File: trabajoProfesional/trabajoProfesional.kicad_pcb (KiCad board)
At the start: 2 copper layers, 66.2 x 25.4 mm, 47 parts, among them T1 MPMOS, U1 1501

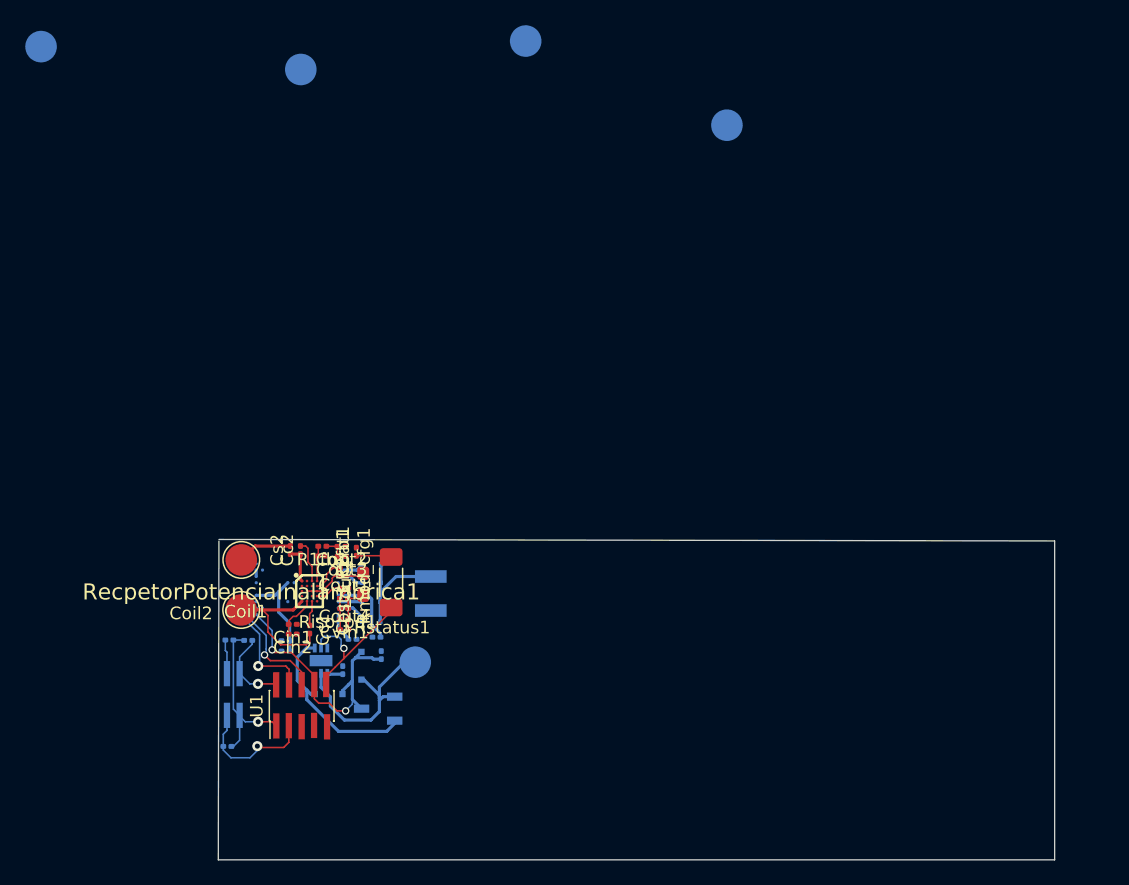
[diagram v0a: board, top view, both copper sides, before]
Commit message: fue todo a doble capa con componentes de dos lados
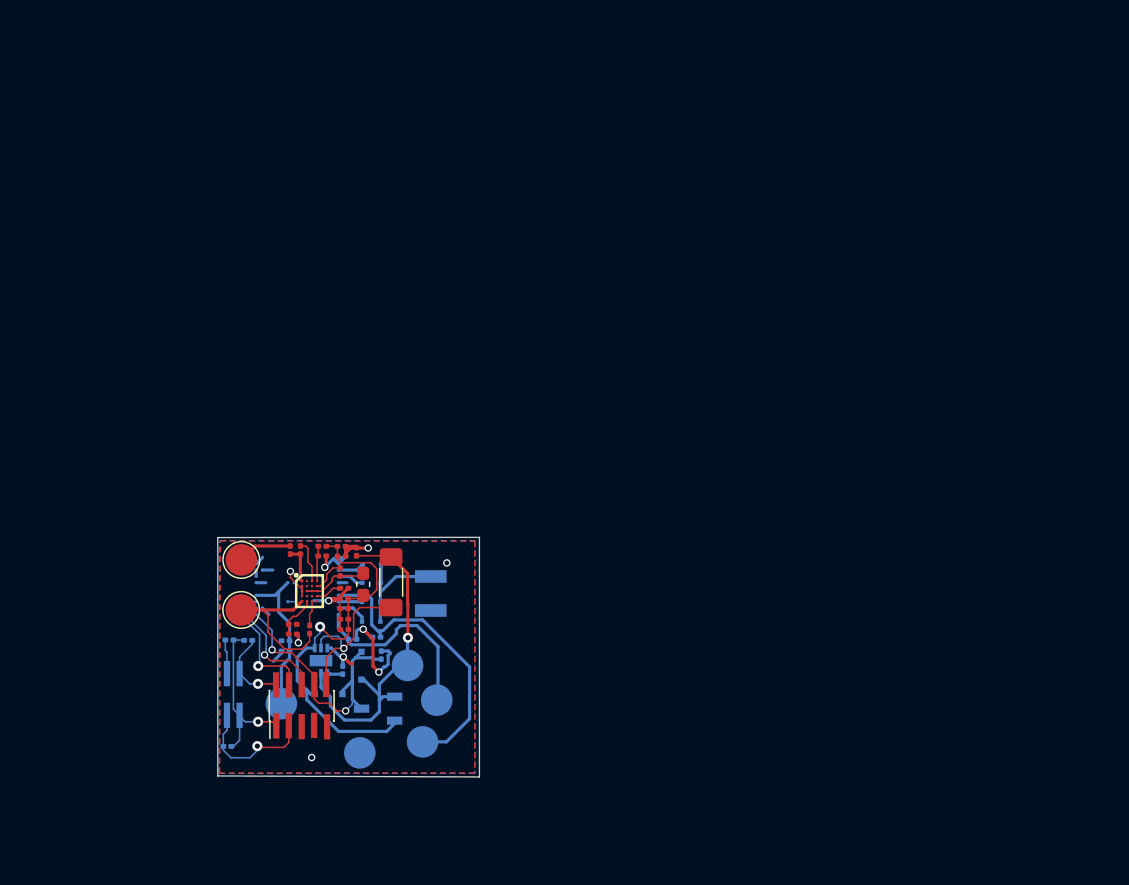
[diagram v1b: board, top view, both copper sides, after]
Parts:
- removed Cbst1: 47n, Capacitor_SMD:C_0201_0603Metric
- removed Cc2: 1n, Capacitor_SMD:C_0201_0603Metric
- removed Coil2, HV-1: Conn_01x01_Male, TestPoint:TestPoint_Pad_D2.5mm
- removed Cout1, Cout4: 22u, Capacitor_SMD:C_0201_0603Metric
- removed Riso_pd1: R, Resistor_SMD:R_0201_0603Metric
- removed Rmod_cfg1: 60k, Resistor_SMD:R_0201_0603Metric
- added  : 60k, Resistor_SMD:R_0201_0603Metric, F.Cu at (68.3, 63.0)
- added  : 22u, Capacitor_SMD:C_0201_0603Metric, F.Cu at (68.3, 63.8)
- added  : 1n, Capacitor_SMD:C_0201_0603Metric, F.Cu at (64.8, 59.9)
- added  : R, Resistor_SMD:R_0201_0603Metric, F.Cu at (68.3, 64.6)
- added  : 47n, Capacitor_SMD:C_0201_0603Metric, F.Cu at (68.0, 61.7)
- added  : Conn_01x01_Male, TestPoint:TestPoint_Pad_D2.5mm, B.Cu at (75.6, 71.8)
- added  : Conn_01x01_Male, TestPoint:TestPoint_Pad_D2.5mm, F.Cu at (60.2, 64.7)
- added  : 22u, Capacitor_SMD:C_0201_0603Metric, F.Cu at (68.3, 66.2)
-  : renamed from Cin2
-  : renamed from Cin1
-  : renamed from Cc1
-  : renamed from Cbat1
-  : renamed from Rstatus1
-  : renamed from DriverPotencia1
-  : renamed from RIPRGM1
-  : renamed from U1
-  : renamed from R2fb1
-  : renamed from R1fb1
-  : renamed from R2
-  : renamed from R1
-  : renamed from C6
-  : renamed from C5
-  : renamed from C4
-  : renamed from C3
-  : renamed from C2
-  : renamed from SensorPresion1
-  : renamed from C1
-  : renamed from AdministracionBateria1
-  : renamed from PiezoElectrico1
-  : renamed from HV+1
-  : renamed from Coil1
-  : renamed from BatPositivo1
-  : renamed from batGND1
-  : renamed from 10V1
-  : renamed from Lout1
-  : renamed from T1
-  : renamed from RecpetorPotenciaInalambrica1
-  : renamed from opt1
-  : renamed from DbyPass1
-  : renamed from D4
-  : renamed from D3
-  : renamed from D2
-  : renamed from D1
-  : renamed from Cvin1
-  : renamed from Cs2
-  : renamed from Cout3
-  : renamed from Cout2
- moved   57.6 mm to (69.5, 76.0)
- moved   55.4 mm to (63.3, 72.1)
- moved   54.1 mm to (74.5, 75.1)
- moved   0.66 mm to (73.3, 69.1)
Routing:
- net GND: track 3.57 -> 36.3 mm, vias 0 -> 10
- net +HV: track 6.07 -> 23.8 mm
- net -HV: track 2.31 -> 15.5 mm
- net Net-(AdministracionBateria1-Pad1): track 20.1 -> 31.7 mm, vias 0 -> 1
- net +Bat: track 19.4 -> 27.7 mm, vias 0 -> 1
- net 10V: track 7.96 -> 12.4 mm
- net /Bateria/Cargando: track 12.3 -> 13.3 mm
- added copper zone on B.Cu, net GND
- added copper zone on F.Cu, net GND
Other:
- board size 66.2 x 25.4 mm -> 20.7 x 19 mm

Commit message: Add files via upload
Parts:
- removed the   at (68.3, 63.0)
- removed the   at (68.3, 63.8)
- removed the   at (64.2, 66.6)
- removed the   at (64.2, 65.8)
- removed the   at (64.8, 59.9)
- removed the   at (65.6, 66.2)
- removed the   at (69.3, 60.1)
- removed the   at (68.3, 64.6)
- removed the   at (68.2, 69.4)
- removed the   at (66.6, 60.4)
- removed the   at (66.6, 59.6)
- removed the   at (59.1, 75.5)
- removed the   at (60.7, 67.1)
- removed the   at (68.0, 61.7)
- removed the   at (59.2, 67.1)
- removed the   at (70.9, 66.8)
- removed the   at (69.0, 67.0)
- removed the   at (63.7, 67.9)
- removed the   at (71.2, 68.2)
- removed the   at (63.7, 67.1)
- removed the   at (75.6, 71.8)
- removed the   at (74.5, 75.1)
- removed the   at (60.2, 64.7)
- removed the   at (60.2, 60.7)
- removed the   at (73.3, 69.1)
- removed the   at (69.5, 76.0)
- removed the   at (63.3, 72.1)
- removed the   at (69.7, 69.1)
- removed the   at (67.1, 71.3)
- removed the   at (70.5, 61.0)
- removed the   at (70.5, 62.5)
- removed the   at (70.5, 64.0)
- removed the   at (70.5, 65.6)
- removed the   at (68.3, 65.4)
- removed the   at (64.0, 59.9)
- removed the   at (68.3, 66.2)
- removed the   at (68.1, 60.4)
- removed the   at (68.1, 59.6)
- added  : 10n, Capacitor_SMD:C_0201_0603Metric, F.Cu at (61.0, 67.7)
- added  : 22u, Capacitor_SMD:C_0201_0603Metric, F.Cu at (65.5, 64.2)
- added  : 2.2u, Capacitor_SMD:C_0201_0603Metric, F.Cu at (63.9, 64.2)
- added  : 22u, Capacitor_SMD:C_0201_0603Metric, F.Cu at (68.5, 64.4)
- added  : D_Schottky, Diode_SMD:D_SOD-323F, F.Cu at (83.1, 75.5)
- added  : 22u, Capacitor_SMD:C_0201_0603Metric, F.Cu at (66.0, 65.8)
- added  : 10n, Capacitor_SMD:C_0201_0603Metric, F.Cu at (104.0, 70.7)
- added  : 100n, Capacitor_SMD:C_0201_0603Metric, F.Cu at (67.5, 64.4)
- added  : Conn_01x01_Male, TestPoint:TestPoint_Pad_D2.5mm, F.Cu at (106.0, 69.9)
- added  : 1n, Capacitor_SMD:C_0201_0603Metric, F.Cu at (83.5, 67.6)
- added  : R, Resistor_SMD:R_0201_0603Metric, F.Cu at (82.2, 68.6)
- added  : 10k, Resistor_SMD:R_0201_0603Metric, F.Cu at (78.0, 76.4)
- added  : 100n, Capacitor_SMD:C_0201_0603Metric, F.Cu at (85.7, 68.6)
- added  : 10k, Resistor_SMD:R_0201_0603Metric, F.Cu at (85.7, 67.6)
- added  : 10n, Capacitor_SMD:C_0201_0603Metric, F.Cu at (73.5, 70.9)
- added  : 10n, Capacitor_SMD:C_0201_0603Metric, F.Cu at (75.5, 70.9)
- added  : Conn_01x01_Male, TestPoint:TestPoint_Pad_D2.5mm, F.Cu at (108.4, 67.2)
- added  : Conn_01x01_Male, TestPoint:TestPoint_Pad_D2.5mm, F.Cu at (102.3, 63.0)
- added  : D_Schottky, Diode_SMD:D_SOD-323F, F.Cu at (83.2, 73.1)
- added  : 1.8, Diode_SMD:D_SC-80, F.Cu at (65.5, 67.9)
- added  : 1.8, Diode_SMD:D_SC-80, F.Cu at (63.0, 67.9)
- added  : 1.8, Diode_SMD:D_SC-80, F.Cu at (68.0, 67.9)
- added  : 10n, Capacitor_SMD:C_0201_0603Metric, F.Cu at (62.0, 60.7)
- added  : 22u, Capacitor_SMD:C_0201_0603Metric, F.Cu at (93.7, 63.1)
- added  : Conn_01x01_Male, TestPoint:TestPoint_Pad_D2.5mm, F.Cu at (107.2, 63.9)
- added  : 22u, Capacitor_SMD:C_0201_0603Metric, F.Cu at (63.0, 63.0)
- added  : 1n, Capacitor_SMD:C_0201_0603Metric, F.Cu at (63.0, 60.7)
- added  : 2.2u, Capacitor_SMD:C_0201_0603Metric, F.Cu at (95.7, 63.6)
- added  : 10k, Resistor_SMD:R_0201_0603Metric, F.Cu at (91.7, 63.1)
- added  : 46k, Resistor_SMD:R_0201_0603Metric, F.Cu at (62.0, 63.0)
- added  : 47n, Capacitor_SMD:C_0201_0603Metric, F.Cu at (62.0, 64.4)
- added  : Conn_01x01_Male, TestPoint:TestPoint_Pad_D2.5mm, F.Cu at (71.7, 60.1)
- added  : 1.8, Diode_SMD:D_SC-80, F.Cu at (96.0, 66.0)
- added  : R, Resistor_SMD:R_0201_0603Metric, F.Cu at (64.7, 64.2)
- added  : 10n, Capacitor_SMD:C_0201_0603Metric, F.Cu at (74.5, 70.9)
- added  : 60k, Resistor_SMD:R_0201_0603Metric, F.Cu at (66.3, 64.2)
- added  : Conn_01x01_Male, TestPoint:TestPoint_Pad_D2.5mm, F.Cu at (78.7, 60.1)
- added  : Conn_01x01_Male, TestPoint:TestPoint_Pad_D2.5mm, F.Cu at (78.5, 70.4)
-  : moved to F.Cu (x5)
- moved   29.4 mm to (88.7, 67.8), turned to 270 degrees
- moved   22.4 mm to (93.2, 69.6)
- moved   16.8 mm to (83.2, 70.6), turned to 180 degrees
- moved   12.4 mm to (84.2, 60.1)
- moved   10.3 mm to (65.0, 73.4), turned to 180 degrees
- moved   8.93 mm to (73.5, 74.9), turned to 180 degrees
- moved   7.09 mm to (63.5, 65.9), turned to 180 degrees
- moved   4.10 mm to (73.0, 66.9)
- moved   2.36 mm to (66.0, 60.9), turned to 270 degrees
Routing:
- net GND: track 36.3 -> 8.43 mm, vias 10 -> 0
- net +Bat: track 27.7 -> 0.74 mm, vias 1 -> 0
- net +HV: track 23.8 -> 0.00 mm
- net Net-(AdministracionBateria1-Pad1): track 31.7 -> 7.87 mm, vias 1 -> 0
- net /Salida/Alimentacion: track 22.9 -> 0.00 mm, vias 2 -> 0
- net /Bateria/Cargando: track 13.3 -> 0.00 mm, vias 1 -> 0
- net -HV: track 15.5 -> 3.23 mm
- net Net-(Cc1-Pad2): track 11.8 -> 0.00 mm
- net 10V: track 12.4 -> 1.00 mm
- net Net-(C6-Pad2): track 13.1 -> 2.99 mm, vias 1 -> 0
- net /Salida/SN1ONOFF: track 9.96 -> 0.75 mm, vias 1 -> 0
- net SCLPresion: track 10.4 -> 3.00 mm, vias 1 -> 0
- net SDAPresion: track 6.31 -> 0.00 mm, vias 1 -> 0
- net Net-(D1-Pad2): track 9.09 -> 4.32 mm
- net Net-(Coil1-Pad1): track 4.34 -> 0.00 mm
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- removed copper zone on B.Cu, net GND
- removed copper zone on F.Cu, net GND
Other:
- board size 20.7 x 19 mm -> 0.1 x 19.2 mm

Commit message: mira como ponemos todo de una cara
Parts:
- removed  : 22u, Capacitor_SMD:C_0201_0603Metric
- removed  : D_Schottky, Diode_SMD:D_SOD-323F
- removed  : Conn_01x01_Male, TestPoint:TestPoint_Pad_D2.5mm
- added 10V1: Conn_01x01_Male, TestPoint:TestPoint_Pad_D2.5mm, B.Cu at (113.5, 63.9)
- added Cout1: 22u, Capacitor_SMD:C_0201_0603Metric, F.Cu at (69.6, 64.3)
- added opt1: D_Schottky, Diode_SMD:D_SOD-323F, F.Cu at (78.0, 68.8)
- AdministracionBateria1, C1, C2, C3, C4, C5, C6, Cbat1, Cbst1, Cc1, Cc2, Cin1, Cin2, Coil1, Coil2, Cout2, Cout3, Cout4, Cs2, Cvin1, D1, D2, D3, D4, DbyPass1, DriverPotencia1, Lout1, R1, R1fb1, R2, R2fb1, RIPRGM1, RecpetorPotenciaInalambrica1, Riso_pd1, Rmod_cfg1, T1, U1: renamed from  
- BatPositivo1, HV+1, HV-1, PiezoElectrico1, SensorPresion1, batGND1: renamed from  ; moved to B.Cu
- Rstatus1: renamed from  ; footprint Resistor_SMD:R_1806_4516Metric -> Resistor_SMD:R_0201_0603Metric
- moved C1 53.1 mm to (128.3, 77.0)
- moved C3 53.1 mm to (127.3, 77.0)
- moved C5 53.1 mm to (126.3, 77.0)
- moved PiezoElectrico1 34.8 mm to (105.7, 55.0)
- moved SensorPresion1 34.3 mm to (122.8, 64.1), turned to 90 degrees
- moved R2fb1 22.5 mm to (69.2, 63.0)
- moved Cc1 21.5 mm to (62.9, 61.4), turned to 0 degrees
- moved HV+1 13.3 mm to (112.0, 76.2)
- moved batGND1 12.8 mm to (112.5, 70.6)
- moved AdministracionBateria1 12.5 mm to (70.7, 70.0), turned to 90 degrees
- moved R1 12.3 mm to (77.2, 76.5), turned to 90 degrees
- moved HV-1 12.1 mm to (117.0, 58.7)
- moved Rstatus1 11.5 mm to (75.0, 67.0)
- moved DbyPass1 11.5 mm to (73.0, 70.0), turned to 270 degrees
- moved C6 11.0 mm to (78.0, 76.5), turned to 270 degrees
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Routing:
- net /Salida/Alimentacion: track 0.00 -> 8.88 mm
- net /Salida/SN1ONOFF: track 0.75 -> 8.49 mm
- net Net-(Cc1-Pad1): track 0.00 -> 7.60 mm
- net Net-(AdministracionBateria1-Pad1): track 7.87 -> 13.6 mm
- net SDAPresion: track 0.00 -> 4.21 mm
- net Net-(Cbst1-Pad1): track 1.63 -> 4.89 mm
- net 10V: track 1.00 -> 4.07 mm
- net Net-(Cbst1-Pad2): track 0.00 -> 2.96 mm
- net Net-(Cc2-Pad1): track 0.00 -> 2.81 mm
- net Net-(Cin1-Pad2): track 0.00 -> 2.61 mm
- net Net-(RecpetorPotenciaInalambrica1-PadD4): track 0.00 -> 2.16 mm
- net Net-(Cc2-Pad2): track 0.00 -> 2.07 mm
- net Net-(Cc1-Pad2): track 0.00 -> 2.01 mm
- net /Bateria/Cargando: track 0.00 -> 2.00 mm
- net Net-(AdministracionBateria1-Pad4): track 0.00 -> 1.04 mm
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
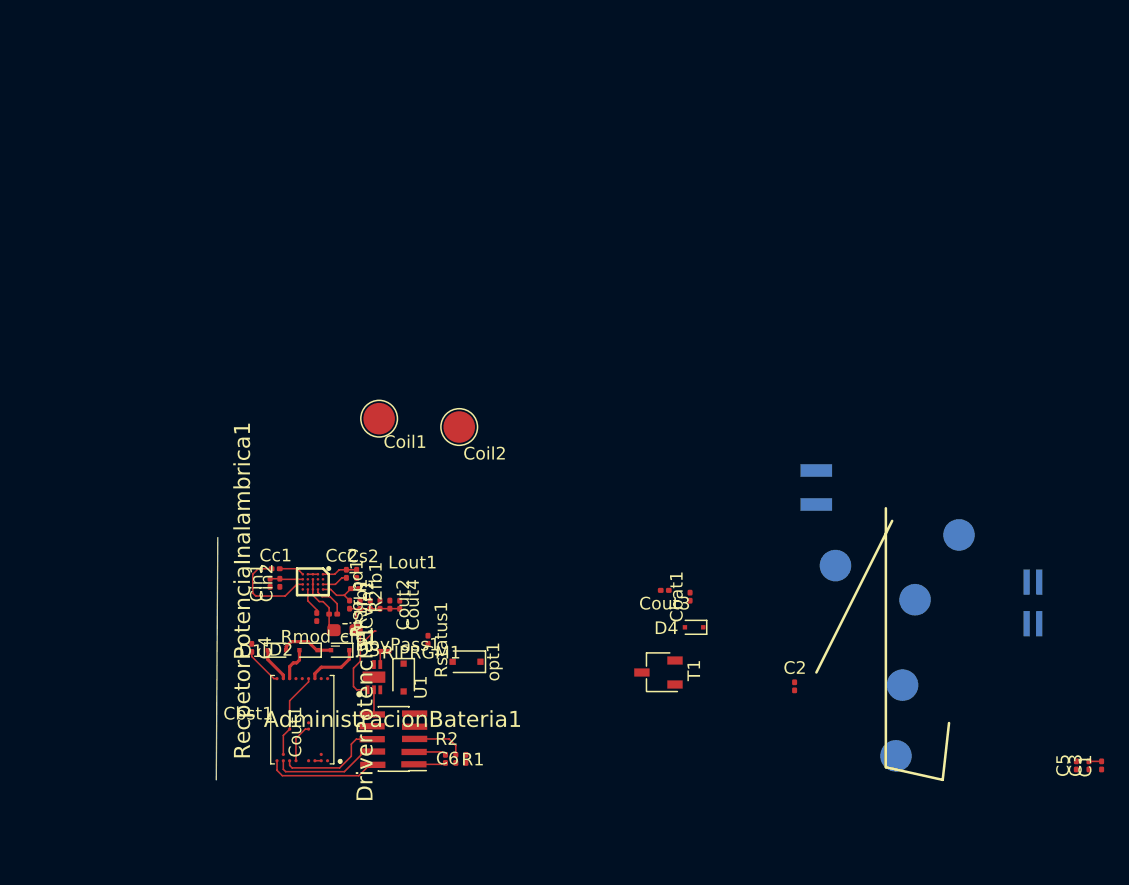
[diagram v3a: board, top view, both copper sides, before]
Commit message: componentes en una capa
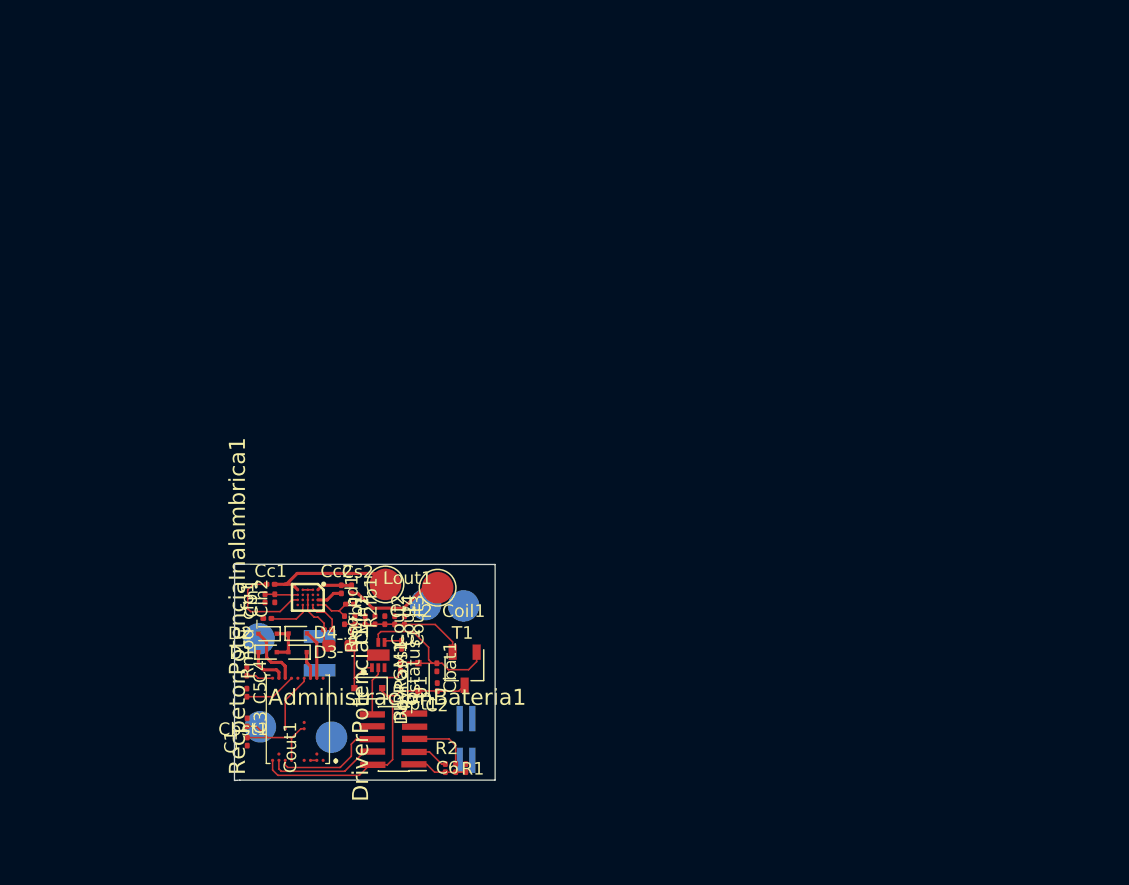
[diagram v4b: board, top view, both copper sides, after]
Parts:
- moved C1 67.7 mm to (60.6, 75.1)
- moved C3 66.7 mm to (60.6, 73.6), turned to 270 degrees
- moved C5 65.9 mm to (60.6, 71.2), turned to 270 degrees
- moved HV-1 56.0 mm to (61.6, 67.0)
- moved HV+1 50.4 mm to (61.7, 73.9)
- moved 10V1 47.5 mm to (67.3, 74.7)
- moved SensorPresion1 46.2 mm to (78.0, 74.9), turned to 270 degrees
- moved PiezoElectrico1 41.4 mm to (66.4, 68.1)
- moved batGND1 38.3 mm to (74.8, 64.2)
- moved D4 31.4 mm to (64.6, 66.5), turned to 0 degrees
- moved BatPositivo1 29.6 mm to (77.8, 64.3)
- moved C2 28.3 mm to (75.7, 70.8), turned to 90 degrees
- moved Cbat1 20.8 mm to (75.7, 69.2), turned to 270 degrees
- moved Cout3 20.7 mm to (73.1, 65.5), turned to 270 degrees
- moved T1 15.3 mm to (77.8, 69.3), turned to 270 degrees
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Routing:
- net /Salida/Alimentacion: track 8.88 -> 23.5 mm
- net +Bat: track 0.00 -> 13.9 mm
- net Net-(Cc1-Pad2): track 2.01 -> 10.7 mm
- net Net-(Coil1-Pad1): track 0.00 -> 7.96 mm
- net 10V: track 4.07 -> 8.57 mm
- net /Bateria/Cargando: track 2.00 -> 6.30 mm
- net +HV: track 0.00 -> 4.14 mm
- net Net-(D4-Pad2): track 0.00 -> 3.89 mm
- net Net-(AdministracionBateria1-Pad1): track 13.6 -> 17.0 mm
- net GND: track 7.63 -> 5.42 mm
- net Net-(D2-Pad2): track 2.72 -> 4.87 mm
- net Net-(D3-Pad1): track 4.31 -> 2.19 mm
- net Net-(C6-Pad2): track 2.55 -> 4.37 mm
- net Net-(RecpetorPotenciaInalambrica1-PadD4): track 2.16 -> 3.31 mm
- net -HV: track 3.08 -> 2.12 mm
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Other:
- board size 0.1 x 19.2 mm -> 20.6 x 17.1 mm
